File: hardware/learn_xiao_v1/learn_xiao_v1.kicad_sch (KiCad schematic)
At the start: 28 parts, among them J1 P0, J10 Conn_02x02_Odd_Even, J2 P1, J3 IO, J4 Conn_02x02_Odd_Even, J5 TYPE-C-31-M-12, J6 GY-87_10DOF, J7 Conn_02x08_Odd_Even, J8 Conn_02x05_Odd_Even, J9 Pot, SW1 SW_Push, SW2 SW_Push, U1 XIAO-SMD, U2 CH340N, U3 W25Q32JVSS, U4 OLED096, U5 LM35-LP

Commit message: added webapp for pdm
added webapp for pdm
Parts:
- removed J10: Conn_02x02_Odd_Even, symbol Connector_Generic:Conn_02x02_Odd_Even
- added J10: Conn_02x03_Odd_Even, symbol Connector_Generic:Conn_02x03_Odd_Even
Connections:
- net +3.3V: now also J9.2 (Pin_2), J9.4 (Pin_4)
- net A1_D1: now also J10.1 (Pin_1)
- net A2_D2: now also J10.3 (Pin_3)
- net A3_D3: now also J10.5 (Pin_5)
- net LM35_OUT: now also J10.2 (Pin_2)
- net 3V3 renamed POT1_OUT
- net POT1_OUT: now also J10.4 (Pin_4); no longer J9.4 (Pin_4)
- net POT_OUT renamed POT2_OUT
- net POT2_OUT: now also J10.6 (Pin_6); no longer J9.2 (Pin_2)
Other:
- moved on the sheet: J9, U5

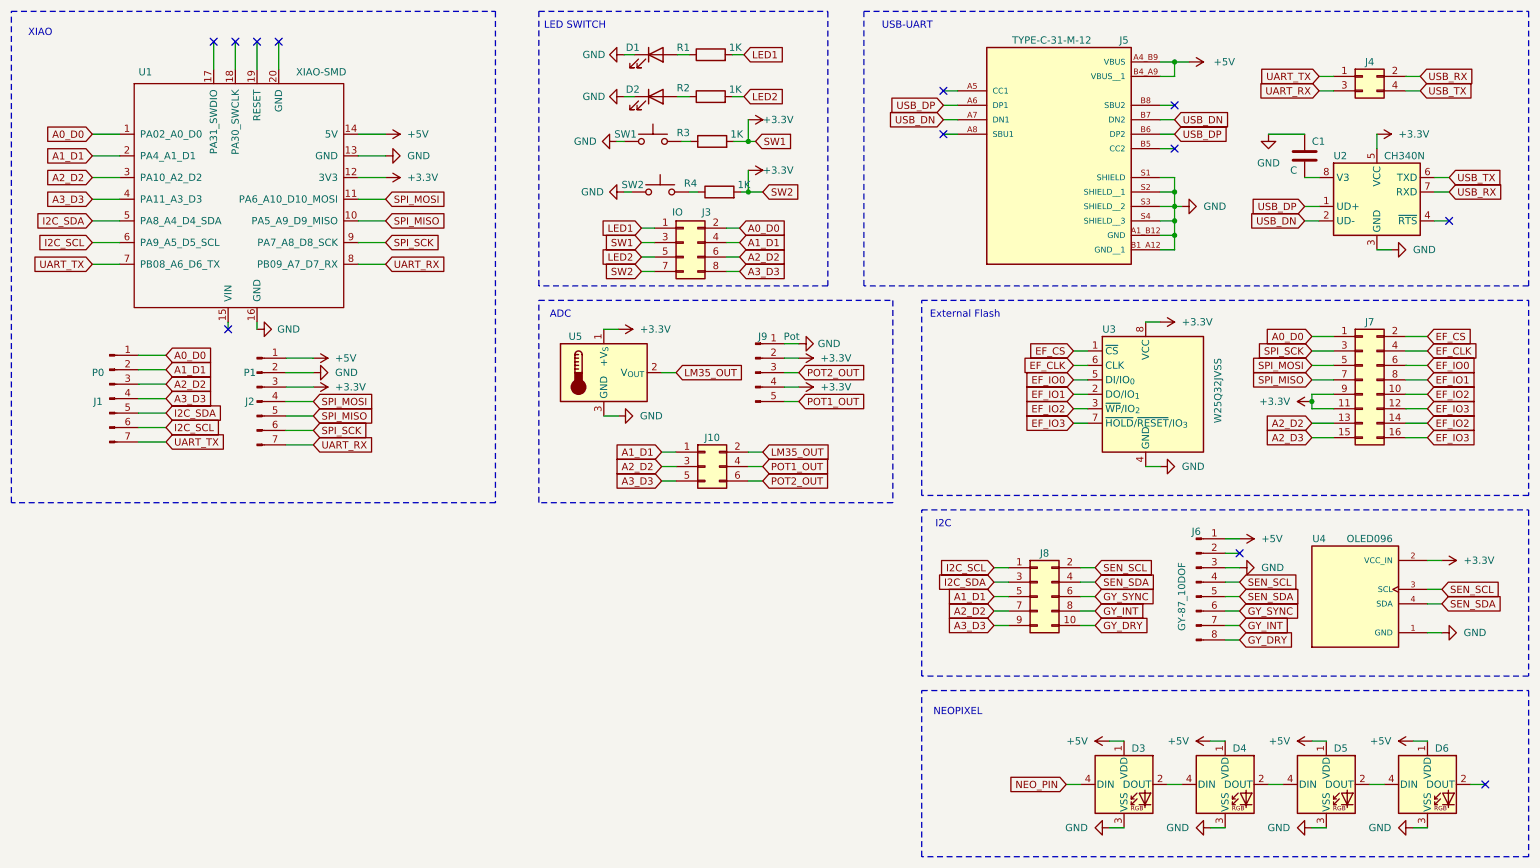
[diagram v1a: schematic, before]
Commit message: added imu, flash, mic samples
added imu, flash, mic samples
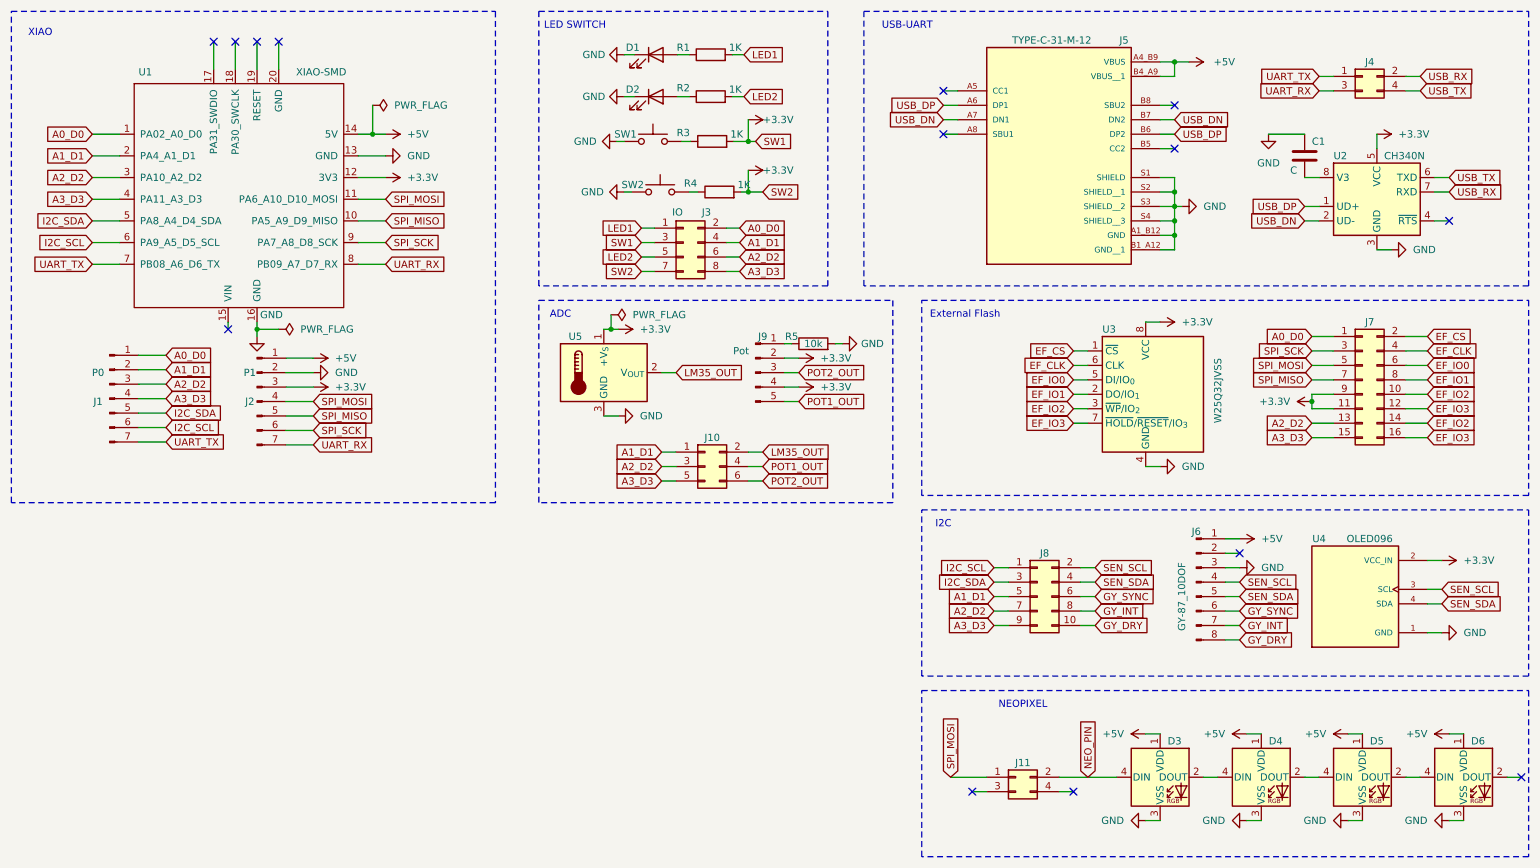
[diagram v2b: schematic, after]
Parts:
- added J11: Conn_02x02_Odd_Even, symbol Connector_Generic:Conn_02x02_Odd_Even
- added R5: 10k, symbol Device:R
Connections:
- net A2_D3 is gone; now on net A3_D3: J7.15 (Pin_15)
- net GND: now also R5.2; no longer J9.1 (Pin_1)
- net NEO_PIN: now also J11.2 (Pin_2)
- net SPI_MOSI: now also J11.1 (Pin_1)
- new net: J9.1 (Pin_1), R5.1
- no-connect marks 12 -> 14
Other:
- moved on the sheet: D3, D4, D5, D6
